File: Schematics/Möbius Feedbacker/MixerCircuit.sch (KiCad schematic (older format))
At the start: 10 parts

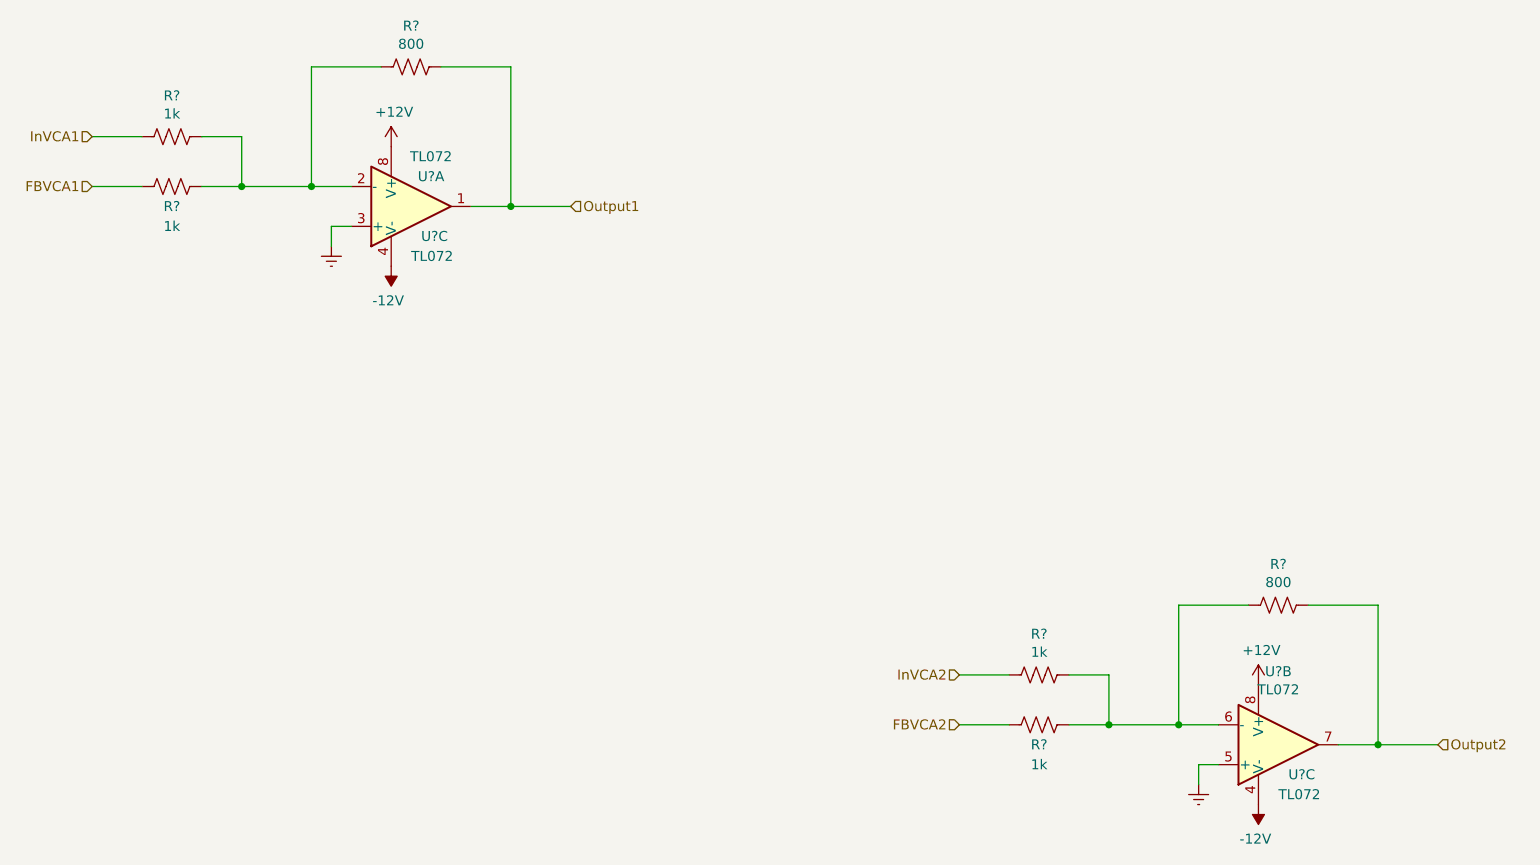
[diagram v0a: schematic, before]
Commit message: Add schematic pdfs, change name to Pathway, update README
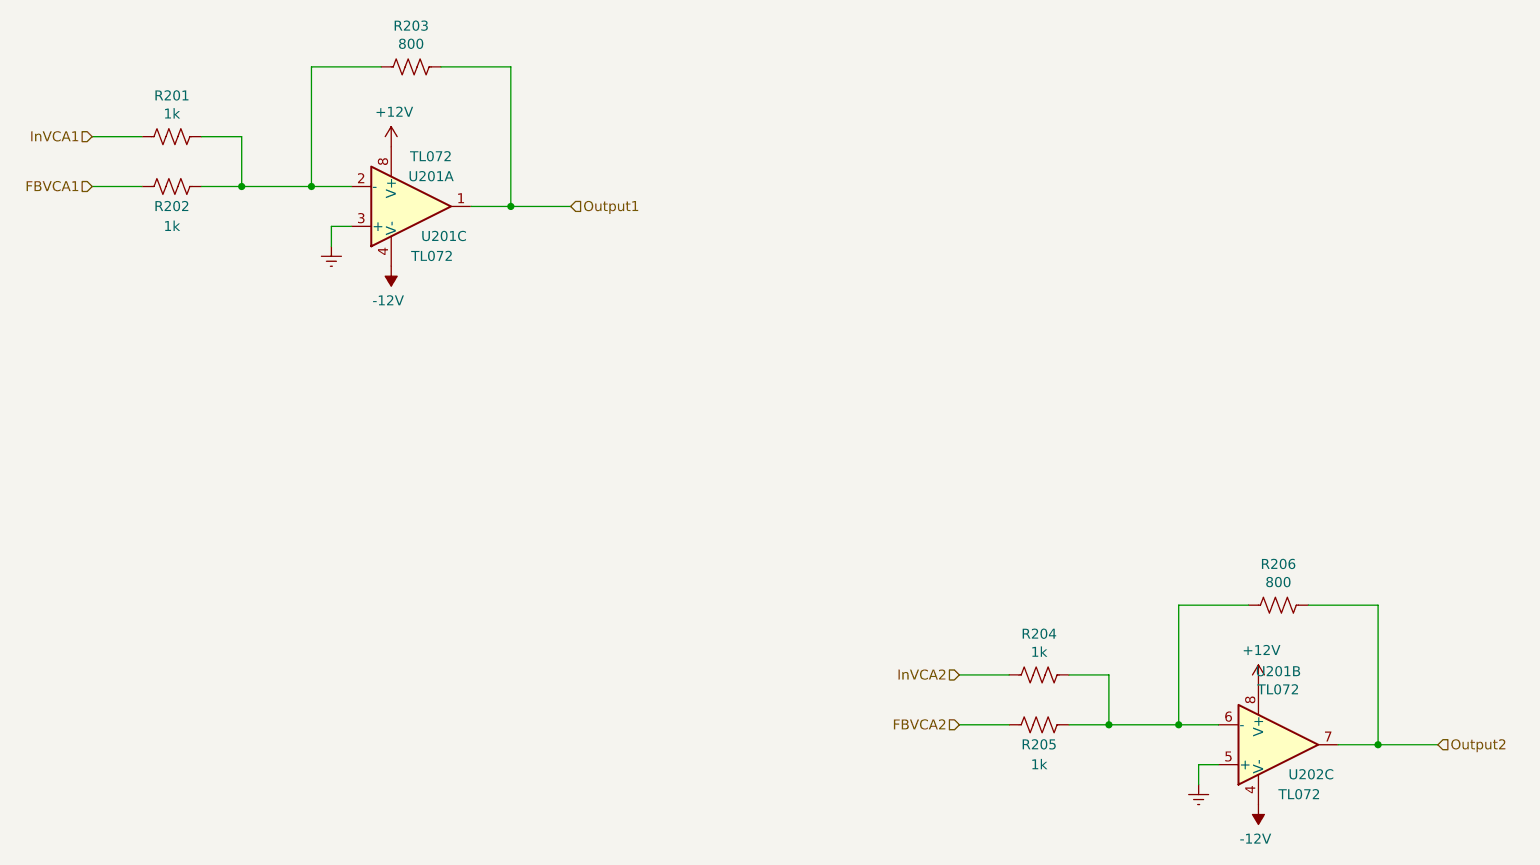
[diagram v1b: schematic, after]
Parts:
- gave numbers to parts that had none: 8
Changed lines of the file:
@@
 Output1
 $Comp
-L power:+12V #PWR?
+L power:+12V #PWR0202
 U 1 1 5E3F8D2B
 P 4100 2150
+AR Path="/5E3F1FBB/5E3F8D2B" Ref="#PWR0202"  Part="1"
+AR Path="/5E26B18F/5E3F8D2B" Ref="#PWR?"  Part="1"
 F 0 "#PWR?" H 4100 2000 50  0001 C CNN
 F 1 "+12V" H 4115 2323 50  0000 C CNN
@@
 $EndComp
 $Comp
-L power:-12V #PWR?
+L power:-12V #PWR0203
 U 1 1 5E3F9114
 P 4100 2750
+AR Path="/5E3F1FBB/5E3F9114" Ref="#PWR0203"  Part="1"
+AR Path="/5E26B18F/5E3F9114" Ref="#PWR?"  Part="1"
 F 0 "#PWR?" H 4100 2850 50  0001 C CNN
 F 1 "-12V" H 4115 2923 50  0000 C CNN
@@
 $EndComp
 $Comp
-L Device:R_US R?
+L Device:R_US R203
 U 1 1 5E3F9703
 P 4200 1750
+AR Path="/5E3F1FBB/5E3F9703" Ref="R203"  Part="1"
+AR Path="/5E26B18F/5E3F9703" Ref="R?"  Part="1"
 F 0 "R?" V 3995 1750 50  0000 C CNN
 F 1 "800" V 4086 1750 50  0000 C CNN
@@
 $EndComp
 $Comp
-L Device:R_US R?
+L Device:R_US R202
 U 1 1 5E3FCDD0
 P 3000 2350
+AR Path="/5E3F1FBB/5E3FCDD0" Ref="R202"  Part="1"
+AR Path="/5E26B18F/5E3FCDD0" Ref="R?"  Part="1"
 F 0 "R?" V 3100 2350 50  0000 C CNN
 F 1 "1k" V 3200 2350 50  0000 C CNN
@@
 $EndComp
 $Comp
-L Device:R_US R?
+L Device:R_US R201
 U 1 1 5E3FD843
 P 3000 2100
+AR Path="/5E3F1FBB/5E3FD843" Ref="R201"  Part="1"
+AR Path="/5E26B18F/5E3FD843" Ref="R?"  Part="1"
 F 0 "R?" V 2795 2100 50  0000 C CNN
 F 1 "1k" V 2886 2100 50  0000 C CNN
@@
 	3150 2100 3350 2100
 $Comp
-L power:Earth #PWR?
+L power:Earth #PWR0201
 U 1 1 5E400D21
 P 3800 2650
+AR Path="/5E3F1FBB/5E400D21" Ref="#PWR0201"  Part="1"
+AR Path="/5E26B18F/5E400D21" Ref="#PWR?"  Part="1"
 F 0 "#PWR?" H 3800 2400 50  0001 C CNN
 F 1 "Earth" H 3800 2500 50  0001 C CNN
@@
 	3800 2650 3800 2550
 $Comp
-L Amplifier_Operational:TL072 U?
+L Amplifier_Operational:TL072 U201
 U 1 1 5E3F2EDF
 P 4200 2450
+AR Path="/5E3F1FBB/5E3F2EDF" Ref="U201"  Part="1"
+AR Path="/5E26B18F/5E3F2EDF" Ref="U?"  Part="1"
 F 0 "U?" H 4300 2300 50  0000 C CNN
 F 1 "TL072" H 4300 2200 50  0000 C CNN
@@
 $EndComp
 $Comp
-L Amplifier_Operational:TL072 U?
+L Amplifier_Operational:TL072 U201
 U 3 1 5E3F3656
 P 4200 2450
+AR Path="/5E3F1FBB/5E3F3656" Ref="U201"  Part="3"
+AR Path="/5E26B18F/5E3F3656" Ref="U?"  Part="3"
 F 0 "U?" H 4250 2300 50  0000 L CNN
 F 1 "TL072" H 4200 2200 50  0000 L CNN
@@
 Connection ~ 4700 2450
 $Comp
-L power:+12V #PWR?
+L power:+12V #PWR0205
 U 1 1 5E41E785
 P 8450 4850
+AR Path="/5E3F1FBB/5E41E785" Ref="#PWR0205"  Part="1"
+AR Path="/5E26B18F/5E41E785" Ref="#PWR?"  Part="1"
 F 0 "#PWR?" H 8450 4700 50  0001 C CNN
 F 1 "+12V" H 8465 5023 50  0000 C CNN
@@
 $EndComp
 $Comp
-L power:-12V #PWR?
+L power:-12V #PWR0206
 U 1 1 5E41E78F
 P 8450 5450
+AR Path="/5E3F1FBB/5E41E78F" Ref="#PWR0206"  Part="1"
+AR Path="/5E26B18F/5E41E78F" Ref="#PWR?"  Part="1"
 F 0 "#PWR?" H 8450 5550 50  0001 C CNN
 F 1 "-12V" H 8465 5623 50  0000 C CNN
@@
 $EndComp
 $Comp
-L Device:R_US R?
+L Device:R_US R206
 U 1 1 5E41E799
 P 8550 4450
+AR Path="/5E3F1FBB/5E41E799" Ref="R206"  Part="1"
+AR Path="/5E26B18F/5E41E799" Ref="R?"  Part="1"
 F 0 "R?" V 8345 4450 50  0000 C CNN
 F 1 "800" V 8436 4450 50  0000 C CNN
@@
 $EndComp
 $Comp
-L Device:R_US R?
+L Device:R_US R205
 U 1 1 5E41E7A3
 P 7350 5050
+AR Path="/5E3F1FBB/5E41E7A3" Ref="R205"  Part="1"
+AR Path="/5E26B18F/5E41E7A3" Ref="R?"  Part="1"
 F 0 "R?" V 7450 5050 50  0000 C CNN
 F 1 "1k" V 7550 5050 50  0000 C CNN
@@
 $EndComp
 $Comp
-L Device:R_US R?
+L Device:R_US R204
 U 1 1 5E41E7AD
 P 7350 4800
+AR Path="/5E3F1FBB/5E41E7AD" Ref="R204"  Part="1"
+AR Path="/5E26B18F/5E41E7AD" Ref="R?"  Part="1"
 F 0 "R?" V 7145 4800 50  0000 C CNN
 F 1 "1k" V 7236 4800 50  0000 C CNN
@@
 	7500 4800 7700 4800
 $Comp
-L power:Earth #PWR?
+L power:Earth #PWR0204
 U 1 1 5E41E7BA
 P 8150 5350
+AR Path="/5E3F1FBB/5E41E7BA" Ref="#PWR0204"  Part="1"
+AR Path="/5E26B18F/5E41E7BA" Ref="#PWR?"  Part="1"
 F 0 "#PWR?" H 8150 5100 50  0001 C CNN
 F 1 "Earth" H 8150 5200 50  0001 C CNN
@@
 	8150 5350 8150 5250
 $Comp
-L Amplifier_Operational:TL072 U?
+L Amplifier_Operational:TL072 U202
 U 3 1 5E41E7CF
 P 8550 5150
+AR Path="/5E3F1FBB/5E41E7CF" Ref="U202"  Part="3"
+AR Path="/5E26B18F/5E41E7CF" Ref="U?"  Part="3"
 F 0 "U?" H 8600 5000 50  0000 L CNN
 F 1 "TL072" H 8550 4900 50  0000 L CNN
@@
 Connection ~ 9050 5150
 $Comp
-L Amplifier_Operational:TL072 U?
+L Amplifier_Operational:TL072 U201
 U 2 1 5E428A77
 P 8550 5150
+AR Path="/5E3F1FBB/5E428A77" Ref="U201"  Part="2"
+AR Path="/5E26B18F/5E428A77" Ref="U?"  Part="2"
 F 0 "U?" H 8550 4783 50  0000 C CNN
 F 1 "TL072" H 8550 4874 50  0000 C CNN
